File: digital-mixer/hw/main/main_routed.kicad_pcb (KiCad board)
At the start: 4 copper layers, 104.5 x 136.5 mm, 190 parts, among them J1 GCT USB4110-GF-A, J10 MIDI OUT SJ-43514-SMT, J2 LiPo 1S 3000 mAh (з платою за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, J3 IN1 SJ-43514-SMT, J4 IN2 SJ-43514-SMT, J5 IN3 SJ-43514-SMT, J6 IN4 SJ-43514-SMT, J7 MAIN OUT SJ-43514-SMT, J8 AUX OUT SJ-43514-SMT, J9 PHONES SJ-43514-SMT, Q1 AO3401A, SW1 Power 5.8mm DPDT self-lock SMD, SW10 EC12SY ch3.1, SW11 EC12SY ch3.2, SW12 EC12SY ch3.3, SW13 Mute 3 TSF-1266, SW14 EC12SY ch4.1, SW15 EC12SY ch4.2, SW16 EC12SY ch4.3, SW17 Mute 4 TSF-1266, SW18 EC12SY master, SW19 FX1 TSF-1266, SW2 EC12SY ch1.1, SW20 FX2 TSF-1266, SW21 AUX TSF-1266, SW22 SHIFT TSF-1266, SW3 EC12SY ch1.2, SW4 EC12SY ch1.3, SW5 Mute 1 TSF-1266, SW6 EC12SY ch2.1, SW7 EC12SY ch2.2, SW8 EC12SY ch2.3, SW9 Mute 2 TSF-1266, U1 Teensy 4.1, U10 PCM5102A, U11 TPA6132A2, U12 MCP23017-E/SO, U13 MCP23017-E/SO, U14 MCP23017-E/SO, U2 USBLC6-2SC6, U3 TP4056, U4 TPS63802, U5 LP5907MFX-3.3, U6 PCM1865, U7 PCM1865, U8 PCM5102A, U9 PCM5102A

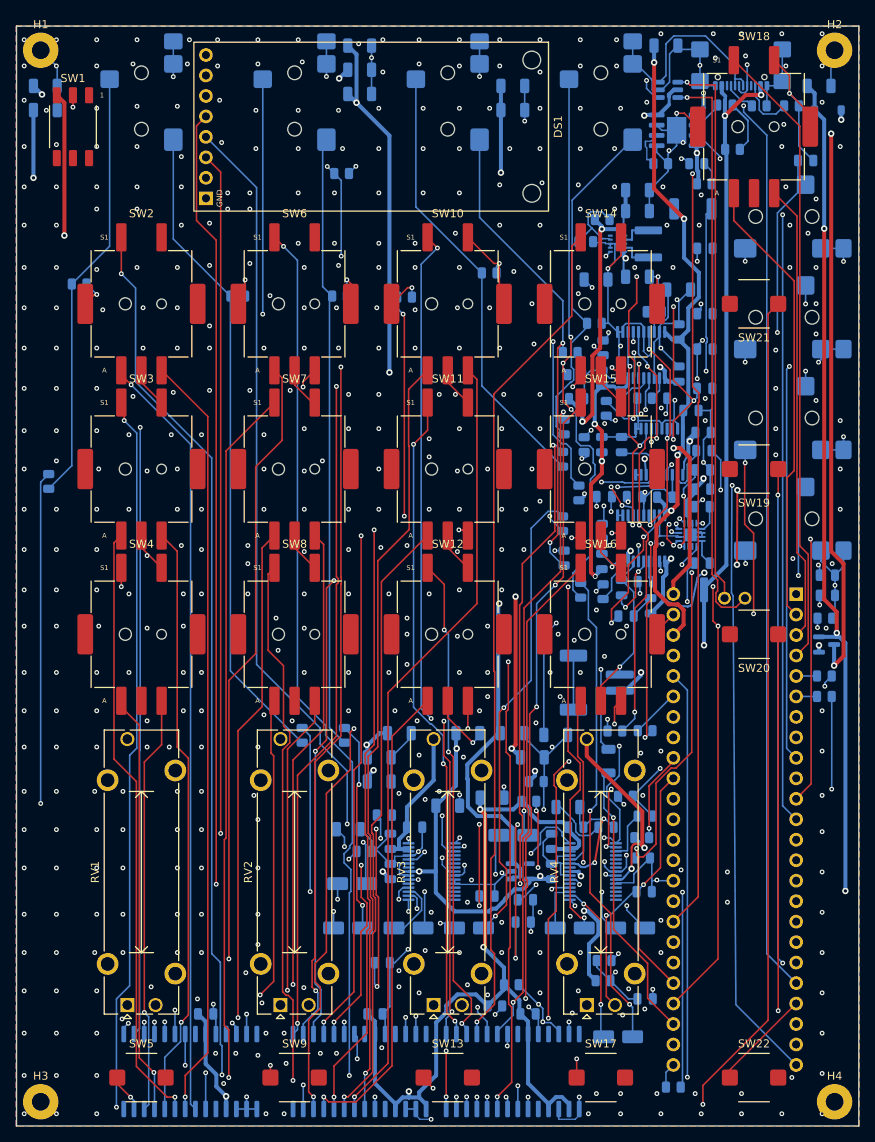
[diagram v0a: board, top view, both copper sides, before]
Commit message: digital-mixer: джеки PJ-327A замість SJ-43514 (DM38)
- footprint, 3D-модель і символ за кресленням продавця AliExpress (площадки 5 × 2 × 3, контакти:
  4 кінчик, 3 кільце, 1 / 2 гільза, 5 перемикач — вільний); креслення HOOYA / XKB / SOFNG — для звірки
- розведена плата: 8 джеків замінено латками, передній торець по краю, носик 2 мм назовні; J8 зсунуто
  на 0,4 мм (напрямна біля кнопки AUX); заборонні зони під нові отвори; DRC 0, розривів 0, схема 0, ERC 0
- джеки — ручний монтаж у всіх варіантах NextPCB (PJ-327A інших виробників мають інші лапки)
- кошик AliExpress на 1 плату: ≈ 400 грн замість 959

Co-Authored-By: Claude Opus 5.5 <noreply@anthropic.com>
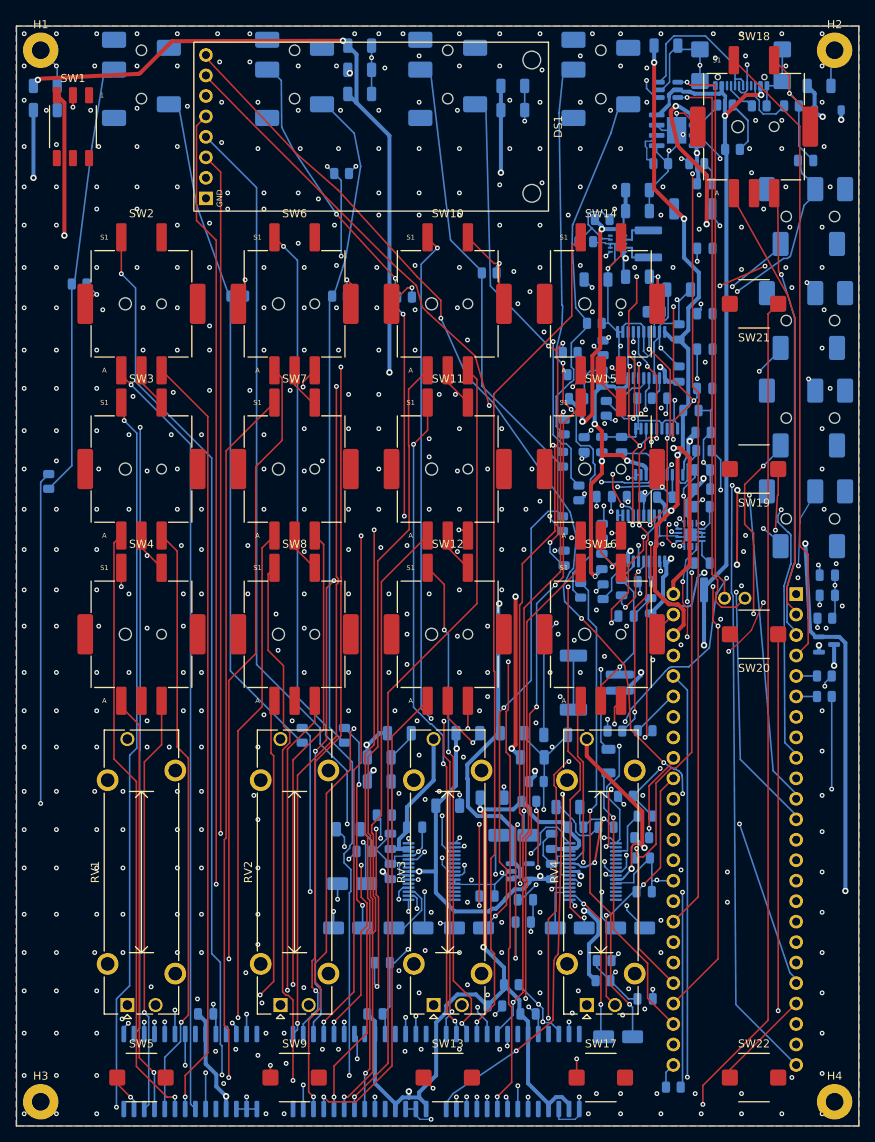
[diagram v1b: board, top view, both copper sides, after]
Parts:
- J10: value MIDI OUT SJ-43514-SMT -> MIDI OUT PJ-327A; footprint pocket-digital:CUI_SJ-43514-SMT_TRRS_Horizontal -> Jack_3.5mm_PJ-327A_SMT_Horizontal
- J3: value IN1 SJ-43514-SMT -> IN1 PJ-327A; footprint pocket-digital:CUI_SJ-43514-SMT_TRRS_Horizontal -> Jack_3.5mm_PJ-327A_SMT_Horizontal
- J4: value IN2 SJ-43514-SMT -> IN2 PJ-327A; footprint pocket-digital:CUI_SJ-43514-SMT_TRRS_Horizontal -> Jack_3.5mm_PJ-327A_SMT_Horizontal
- J5: value IN3 SJ-43514-SMT -> IN3 PJ-327A; footprint pocket-digital:CUI_SJ-43514-SMT_TRRS_Horizontal -> Jack_3.5mm_PJ-327A_SMT_Horizontal
- J6: value IN4 SJ-43514-SMT -> IN4 PJ-327A; footprint pocket-digital:CUI_SJ-43514-SMT_TRRS_Horizontal -> Jack_3.5mm_PJ-327A_SMT_Horizontal
- J7: value MAIN OUT SJ-43514-SMT -> MAIN OUT PJ-327A; footprint pocket-digital:CUI_SJ-43514-SMT_TRRS_Horizontal -> Jack_3.5mm_PJ-327A_SMT_Horizontal
- J8: value AUX OUT SJ-43514-SMT -> AUX OUT PJ-327A; footprint pocket-digital:CUI_SJ-43514-SMT_TRRS_Horizontal -> Jack_3.5mm_PJ-327A_SMT_Horizontal
- J9: value PHONES SJ-43514-SMT -> PHONES PJ-327A; footprint pocket-digital:CUI_SJ-43514-SMT_TRRS_Horizontal -> Jack_3.5mm_PJ-327A_SMT_Horizontal
- moved J8 1.36 mm to (124.5, 56.5), turned to 90 degrees
- moved J10 1.30 mm to (124.5, 68.6), turned to 90 degrees
- moved J3 1.30 mm to (35.5, 20.0), turned to 180 degrees
- moved J4 1.30 mm to (54.5, 20.0), turned to 180 degrees
- moved J5 1.30 mm to (73.5, 20.0), turned to 180 degrees
- moved J6 1.30 mm to (92.5, 20.0), turned to 180 degrees
- moved J7 1.30 mm to (124.5, 43.6), turned to 90 degrees
- moved J9 1.30 mm to (124.5, 81.1), turned to 90 degrees
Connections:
- J10 pad 2: /MIDI_SINK -> /GND
- J10 pad 4: /GND -> /MIDI_SINK
- J3 pad 2: /IN1_T -> /GND
- J3 pad 4: /GND -> /IN1_T
- J4 pad 2: /IN2_T -> /GND
- J4 pad 4: /GND -> /IN2_T
- J5 pad 2: /IN3_T -> /GND
- J5 pad 4: /GND -> /IN3_T
- J6 pad 2: /IN4_T -> /GND
- J6 pad 4: /GND -> /IN4_T
- J7 pad 2: /MAIN_L -> /GND
- J7 pad 4: /GND -> /MAIN_L
- J8 pad 2: /AUX_L -> /GND
- J8 pad 4: /GND -> /AUX_L
- J9 pad 2: /PH_L -> /GND
- J9 pad 4: /GND -> /PH_L
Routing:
- net /GND: track 560.3 -> 521.5 mm, vias 495 -> 497
- net /LCD_BLK: track 180.9 -> 142.2 mm, vias 1 -> 5
- net /LCD_CS: track 154.4 -> 124.9 mm, vias 1 -> 2
- net /BTN_FX1: track 115.0 -> 96.8 mm, vias 4 -> 5
- net /BAT+: track 166.3 -> 148.6 mm
- net /IN2_R: track 94.7 -> 79.7 mm, vias 4 -> 5
- net /MIDI_SRC: track 34.7 -> 24.0 mm
- net /MAIN_R: track 45.4 -> 34.7 mm
- net /PH_R: track 31.7 -> 39.7 mm, vias 2 -> 5
- net /VSYS: track 267.4 -> 261.2 mm
- net /MAIN_L: track 40.1 -> 44.3 mm
- net /ENC_M_A: track 56.2 -> 52.0 mm
- net /ENC_M_B: track 56.9 -> 53.2 mm, vias 0 -> 1
- net /IN3_T: track 59.7 -> 63.4 mm, vias 2 -> 3
- net /IN2_T: track 76.4 -> 80.0 mm
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
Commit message: digital-mixer: фейдери Alps RS201111J011 замість Bourns PTA2043 (DM39)
Footprint і 3D-модель за кресленням № 1 каталогу Alps (і продавця): 3 виводи Ø1,5,
25 і 3,75 мм. Центр ходу на старому місці; на розведеній платі R12/R13/R48 зсунуто,
38 з'єднань проведено заново. ERC 0, DRC 0 порушень, 0 розривів, 0 розбіжностей.

Co-Authored-By: Claude Opus 5.5 <noreply@anthropic.com>
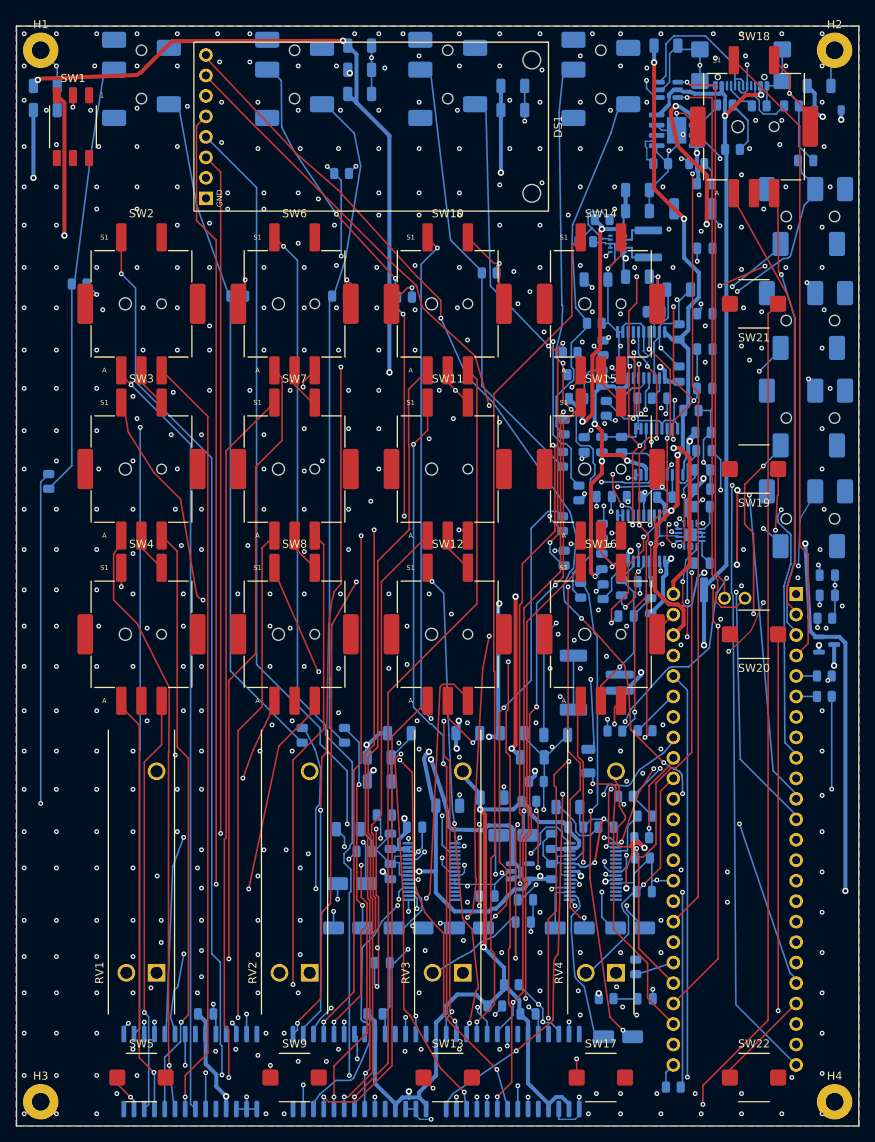
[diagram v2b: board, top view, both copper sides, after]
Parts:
- RV1, RV2, RV3, RV4: value PTA2043 10k B -> RS201111J011 10k B; footprint Potentiometer_THT:Potentiometer_Bourns_PTA2043_Single_Slide -> pocket-digital:Potentiometer_Alps_RS20111_Single_Slide
- moved RV1 5.40 mm to (37.4, 137.5)
- moved RV2 5.40 mm to (56.4, 137.5)
- moved RV3 5.40 mm to (75.4, 137.5)
- moved RV4 5.40 mm to (94.4, 137.5)
- moved R13 4.00 mm to (96.8, 136.7), turned to 90 degrees
- moved R48 2.50 mm to (90.9, 111.2)
- moved R12 2.25 mm to (93.2, 140.7)
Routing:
- net /ENC1_2_SW: track 139.8 -> 104.6 mm
- net /ENC2_3_SW: track 90.0 -> 72.7 mm, vias 2 -> 3
- net /+3V3: track 495.9 -> 480.7 mm, vias 13 -> 15
- net /ENC4_1_A: track 114.6 -> 100.0 mm
- net /ENC4_2_A: track 90.8 -> 77.2 mm, vias 3 -> 4
- net /ENC2_3_B: track 55.3 -> 44.3 mm
- net /ADC_LRCK: track 64.5 -> 55.3 mm, vias 4 -> 5
- net /VBAT_SENSE: track 16.7 -> 7.66 mm, vias 1 -> 0
- net /ENC2_3_A: track 52.2 -> 43.2 mm
- net /+4V2: track 150.8 -> 159.2 mm, vias 5 -> 7
- net /ENC1_2_A: track 75.2 -> 70.8 mm
- net /ENC3_3_B: track 67.9 -> 63.5 mm, vias 3 -> 2
- net /IN1_LS: track 39.5 -> 35.2 mm
- net /FADER4: track 32.5 -> 28.3 mm, vias 2 -> 1
- net /+3V3A: track 317.3 -> 321.1 mm, vias 21 -> 23
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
